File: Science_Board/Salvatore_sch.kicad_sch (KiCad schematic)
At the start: 7 parts, among them U3 PCA9685PW

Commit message: EFuses
They done
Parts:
- removed U3: PCA9685PW, Package_SO:TSSOP-28_4.4x9.7mm_P0.65mm, symbol Driver_LED:PCA9685PW
- added U5: PCA9685BS, Package_DFN_QFN:QFN-28-1EP_6x6mm_P0.65mm_EP4.25x4.25mm, symbol Driver_LED:PCA9685BS
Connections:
- net GND: now also U5.11 (VSS), U5.29 (VSS)
- net Serial Clock: now also U5.23 (SCL)
- net Serial Data: now also U5.24 (SDA)
- net Servo: now also U5.10 (LED7), U5.3 (LED0), U5.4 (LED1), U5.5 (LED2), U5.6 (LED3), U5.7 (LED4), U5.8 (LED5), U5.9 (LED6)
- new net VCC: U5.25 (VDD)
- no-connect marks 8 -> 0
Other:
- moved on the sheet: D2, D3, D4, R2, R3, R4

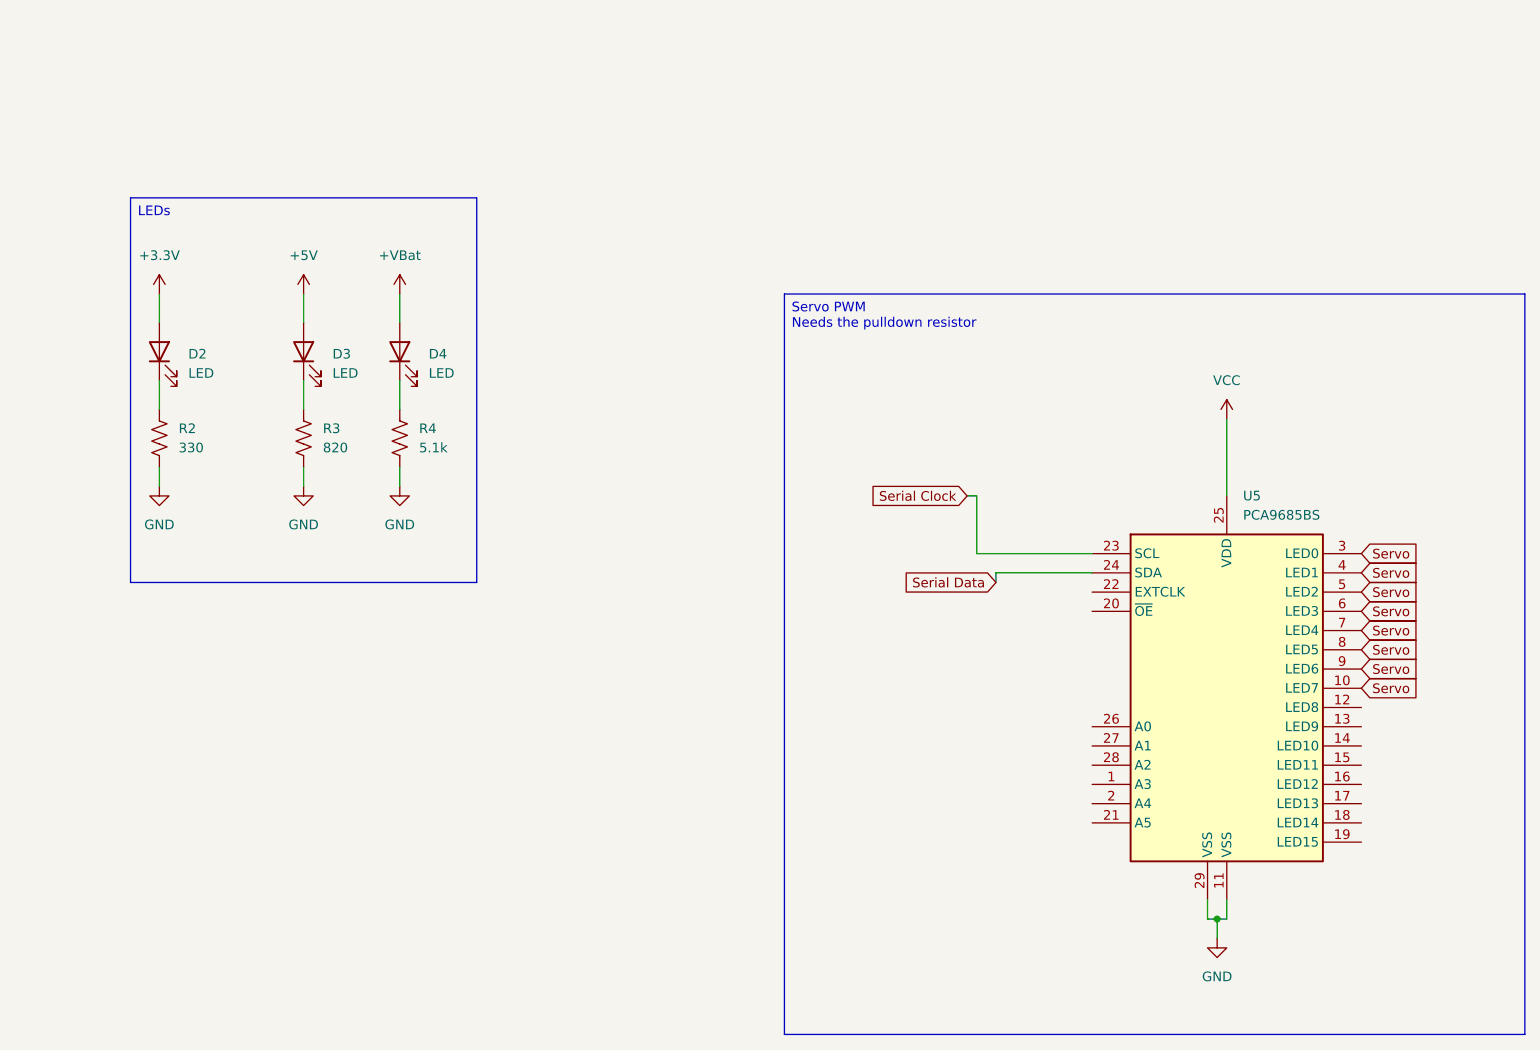
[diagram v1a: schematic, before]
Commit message: changed to right board and put correct inputs into some parts
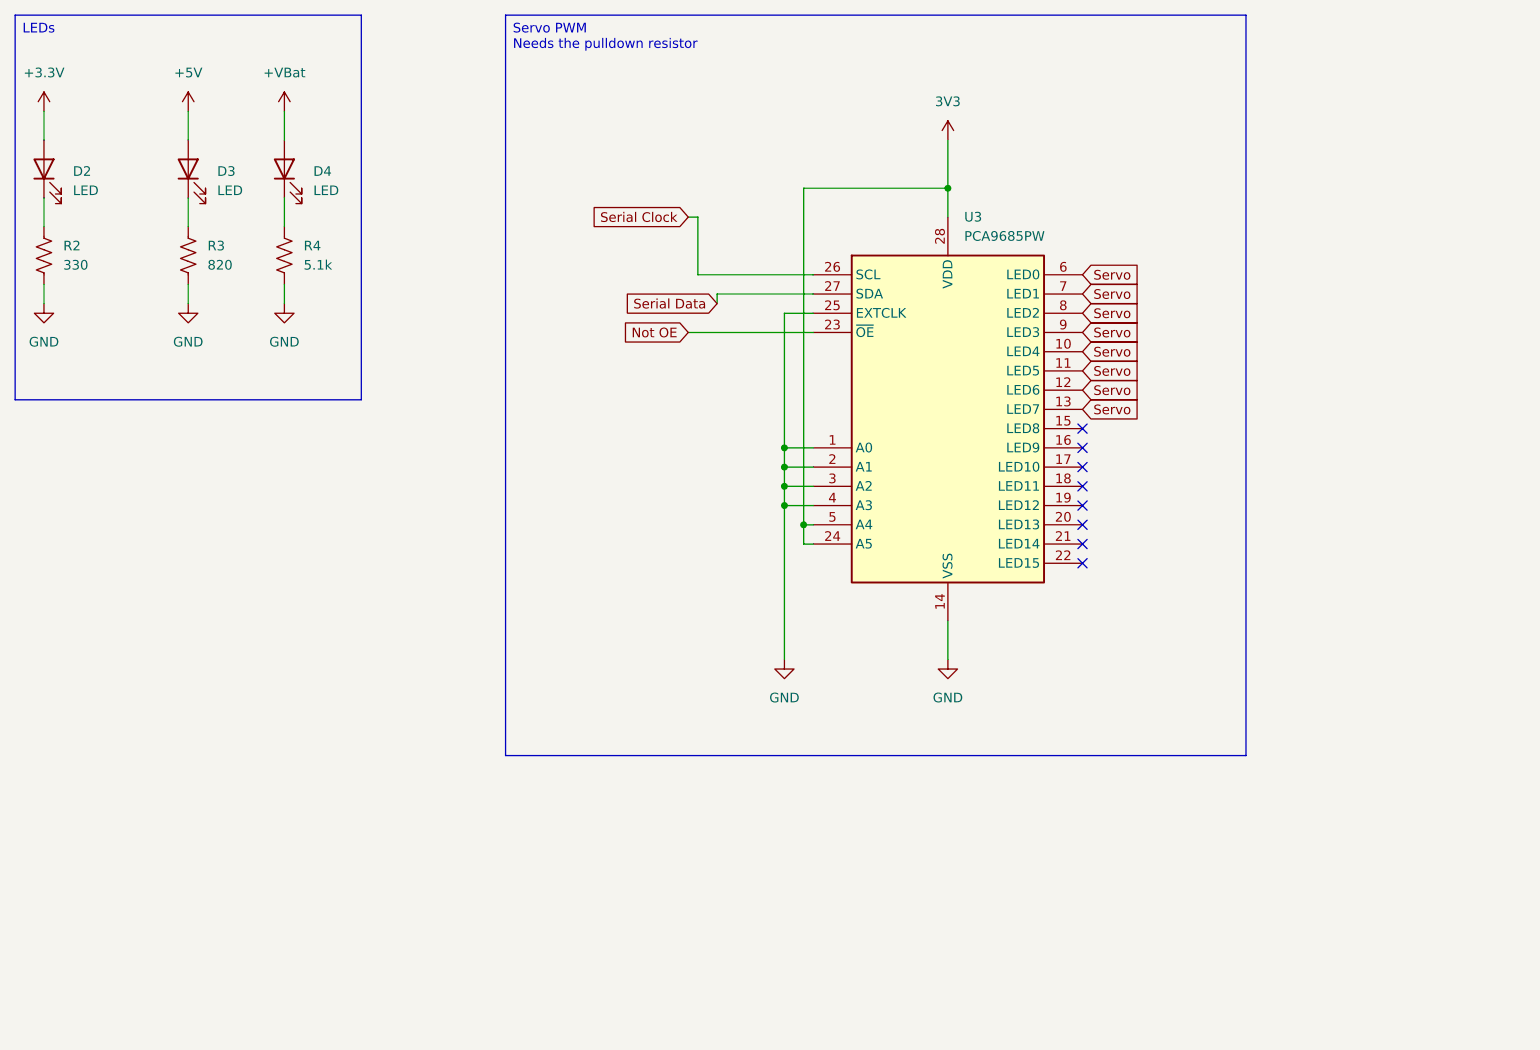
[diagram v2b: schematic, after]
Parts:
- removed U5: PCA9685BS, Package_DFN_QFN:QFN-28-1EP_6x6mm_P0.65mm_EP4.25x4.25mm, symbol Driver_LED:PCA9685BS
- added U3: PCA9685PW, Package_SO:TSSOP-28_4.4x9.7mm_P0.65mm, symbol Driver_LED:PCA9685PW
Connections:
- net GND: now also U3.1 (A0), U3.14 (VSS), U3.2 (A1), U3.25 (EXTCLK), U3.3 (A2), U3.4 (A3)
- net Serial Clock: now also U3.26 (SCL)
- net Serial Data: now also U3.27 (SDA)
- net Servo: now also U3.10 (LED4), U3.11 (LED5), U3.12 (LED6), U3.13 (LED7), U3.6 (LED0), U3.7 (LED1), U3.8 (LED2), U3.9 (LED3)
- new net 3V3: U3.24 (A5), U3.28 (VDD), U3.5 (A4)
- new net Not OE: U3.23 (~{OE})
- no-connect marks 0 -> 8
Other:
- moved on the sheet: D2, D3, D4, R2, R3, R4
